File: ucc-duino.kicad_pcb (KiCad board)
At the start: 2 copper layers, 68.6 x 53.3 mm, 61 parts, among them J1 USB_OTG, J1-A1 Con1x8F, J1-B1 Con1x8F, J2 Con1x6F, J3 Con1x2F, J3-A1 Con1x8F, J3-B1 Con1x8F, J4 Con1x6F, J5 Con2x2CClocw, P5 CONN_01X01, P6 CONN_01X01, P7 CONN_01X01, P8 CONN_01X01, Q1 BC817, Q2 BC817, SW1 SW_Push, SW2 SW_Push, SW3 SW_USR, U1 STM32F103R4T6, U2 AP1117-33, Y1 OSC 8MHz, Y2 OSC 32768KHz

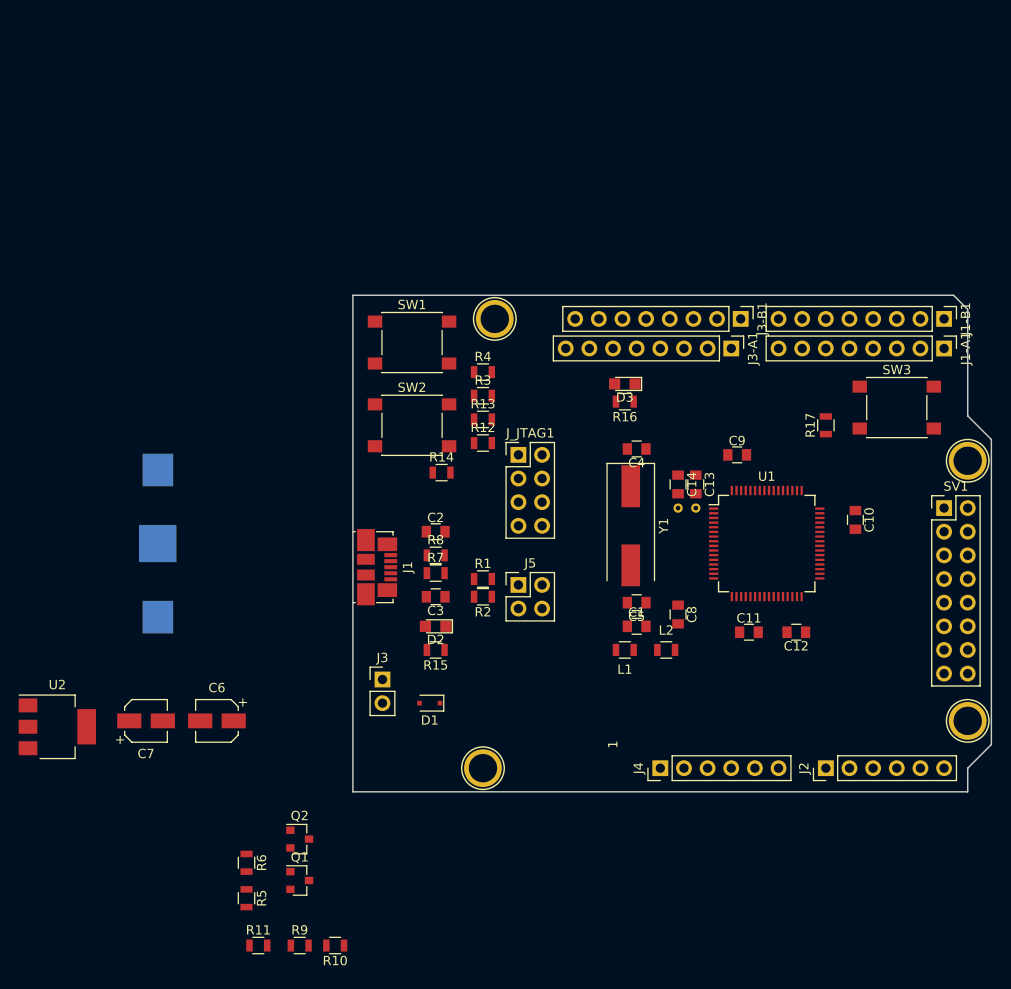
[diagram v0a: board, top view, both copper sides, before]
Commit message: Primeras pistas y leve reacomodación de componentes
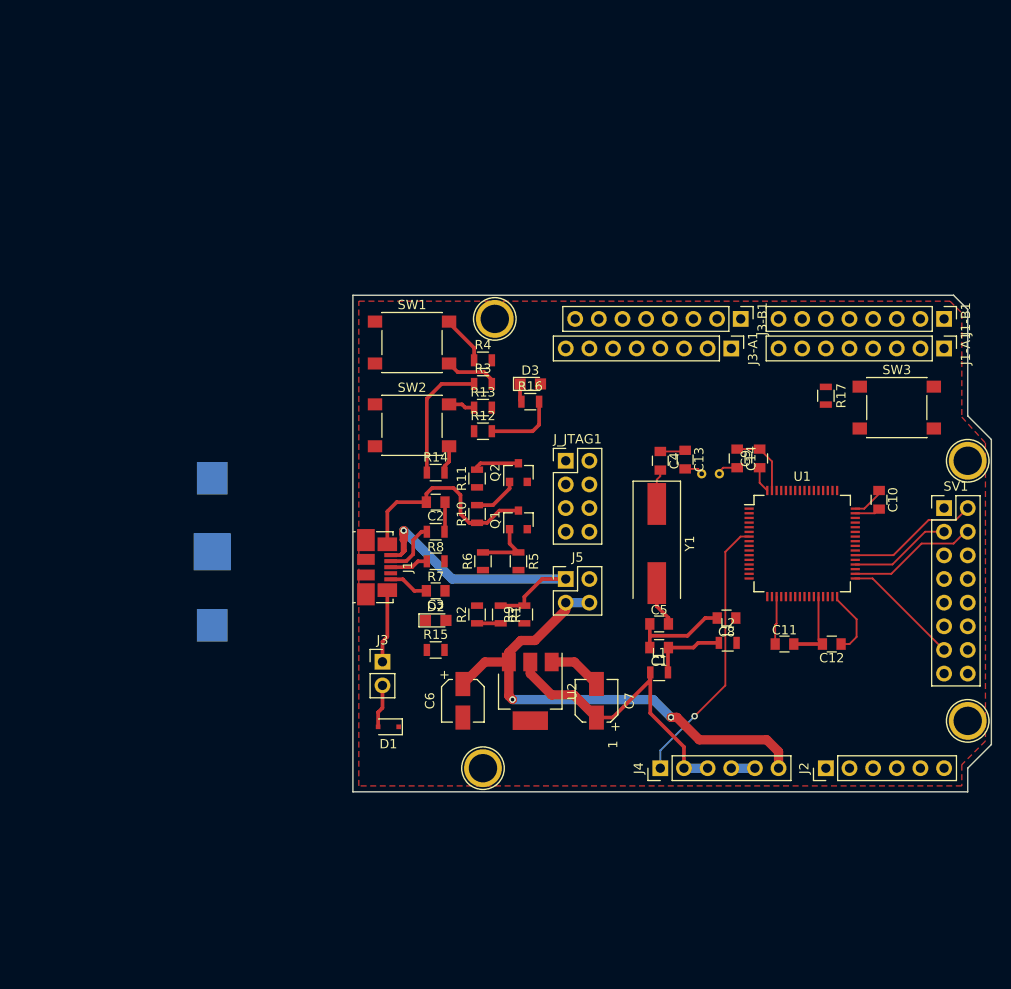
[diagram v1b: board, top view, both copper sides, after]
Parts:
- moved R11 55.4 mm to (123.7, 92.1), turned to 90 degrees
- moved U2 50.9 mm to (129.4, 114.9), turned to 270 degrees
- moved R10 48.8 mm to (123.7, 95.9), turned to 90 degrees
- moved C7 48.4 mm to (136.5, 116.0), turned to 90 degrees
- moved R5 46.5 mm to (128.1, 101.0)
- moved Q2 45.8 mm to (128.1, 91.4), turned to 90 degrees
- moved Q1 45.3 mm to (128.1, 96.5), turned to 90 degrees
- moved R9 43.0 mm to (128.8, 106.7), turned to 90 degrees
- moved R6 41.2 mm to (124.3, 101.0), turned to 90 degrees
- moved C6 26.5 mm to (122.2, 116.0), turned to 270 degrees
- moved D3 10.2 mm to (129.4, 81.9), turned to 0 degrees
- moved R16 10.2 mm to (129.4, 83.8), turned to 0 degrees
- moved C14 6.94 mm to (151.6, 89.9)
- moved L2 6.65 mm to (150.6, 109.7)
- moved BT1 5.91 mm to (95.2, 99.9), turned to 270 degrees
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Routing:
- net GND: track 0.00 -> 82.7 mm
- net VDD: track 0.00 -> 65.3 mm
- net /Vin: track 0.00 -> 55.1 mm, vias 0 -> 2
- net VBUS: track 0.00 -> 37.4 mm, vias 0 -> 1
- net /JTAG-TRST: track 0.00 -> 35.1 mm, vias 0 -> 1
- net /36: track 0.00 -> 14.2 mm
- net /32: track 0.00 -> 14.0 mm
- net /31: track 0.00 -> 12.7 mm
- net /34: track 0.00 -> 11.0 mm
- net Net-(C1-Pad1): track 0.00 -> 8.31 mm
- net Net-(Q1-Pad1): track 0.00 -> 6.70 mm
- net Net-(J1-Pad2): track 0.00 -> 6.08 mm
- net Net-(R4-Pad1): track 0.00 -> 5.27 mm
- net Net-(Q1-Pad2): track 0.00 -> 4.95 mm
- net Net-(Q2-Pad3): track 0.00 -> 4.92 mm
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- added copper zone on F.Cu, net GND
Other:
- net class 1mm added: clearance 0.3, trace_width 0.4, via_dia 0.8, via_drill 0.4
- net class Default: trace_width 0.25 -> 0.2; via_dia 0.6 -> 0.7
- net class Fino added: clearance 0.2, trace_width 0.2, via_dia 0.7, via_drill 0.4
- net class Mínimo MAYER added: clearance 0.125, trace_width 0.125, via_dia 0.7, via_drill 0.4
- net class normal added: clearance 0.4, trace_width 1, via_dia 1.2, via_drill 0.8
- rule trace_min: 0.2 -> 0.125
- rule via_min_drill: 0.3 -> 0.4
- rule via_min_size: 0.4 -> 0.7

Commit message: Pistas day 3
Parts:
- Y2: moved to F.Cu
- moved BT1 65.8 mm to (140.6, 52.3)
- moved C14 5.97 mm to (145.7, 90.2)
- moved C13 5.97 mm to (152.0, 89.9)
- moved D3 2.75 mm to (131.7, 83.4), turned to 270 degrees
- moved Y2 2.64 mm to (150.0, 93.1), turned to 180 degrees
- moved R2 1.02 mm to (122.7, 106.7)
- moved R16 0.64 mm to (128.9, 83.4), turned to 270 degrees
- turned R15 to 180 degrees
- turned R17 to 180 degrees
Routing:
- net GND: track 82.7 -> 278.3 mm, vias 0 -> 3
- net VDD: track 65.3 -> 164.6 mm
- net Net-(C3-Pad1): track 0.00 -> 77.8 mm, vias 0 -> 3
- net Net-(C2-Pad1): track 3.20 -> 60.0 mm, vias 0 -> 2
- net /BOOT0: track 2.83 -> 53.1 mm
- net Net-(R13-Pad2): track 0.00 -> 49.7 mm, vias 0 -> 2
- net /14: track 0.00 -> 37.5 mm, vias 0 -> 1
- net Net-(D1-Pad1): track 0.00 -> 33.1 mm, vias 0 -> 1
- net /8: track 0.00 -> 32.7 mm, vias 0 -> 1
- net /37: track 0.00 -> 30.2 mm, vias 0 -> 1
- net /JTAG-TRST: track 35.1 -> 63.9 mm
- net /7: track 0.00 -> 28.0 mm, vias 0 -> 1
- net /6: track 0.00 -> 27.8 mm, vias 0 -> 1
- net Net-(Q1-Pad2): track 4.95 -> 31.5 mm
- net /20: track 0.00 -> 24.6 mm, vias 0 -> 1
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
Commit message: Day4
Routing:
- net VDD: track 164.6 -> 185.0 mm, vias 0 -> 1
- net GND: track 278.3 -> 282.7 mm, vias 3 -> 4
- added copper zone on B.Cu, net GND

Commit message: 8 pistas to go
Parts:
- removed J_JTAG1: Con2x4CCw, Pin_Headers:Pin_Header_Straight_2x04_Pitch2.54mm
- added J-JTAG1: Con2x4Odd, Pin_Headers:Pin_Header_Straight_2x04_Pitch2.54mm, F.Cu at (133.2, 89.4)
- SV1: value Con2x8CCw -> Con2x8Odd
- moved SV1 18.0 mm to (176.4, 113.0), turned to 180 degrees
- moved C4 7.69 mm to (147.3, 96.8), turned to 90 degrees
- moved C5 7.54 mm to (147.3, 101.3), turned to 270 degrees
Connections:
- SV1 pad 1: GND -> /23
- SV1 pad 10: /25 -> /32
- SV1 pad 11: /27 -> /33
- SV1 pad 12: /29 -> /34
- SV1 pad 13: /31 -> /35
- SV1 pad 14: /33 -> /36
- SV1 pad 15: /35 -> /37
- SV1 pad 16: /37 -> GND
- SV1 pad 2: /36 -> /24
- SV1 pad 3: /34 -> /25
- SV1 pad 4: /32 -> /26
- SV1 pad 5: /30 -> /27
- SV1 pad 7: /26 -> /29
- SV1 pad 8: /24 -> /30
- SV1 pad 9: /23 -> /31
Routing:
- net GND: track 282.7 -> 371.4 mm, vias 4 -> 6
- net VDD: track 185.0 -> 251.6 mm, vias 1 -> 7
- net /25: track 0.00 -> 57.3 mm, vias 0 -> 1
- net /USB_P: track 3.56 -> 54.4 mm, vias 0 -> 4
- net /23: track 0.00 -> 50.4 mm, vias 0 -> 1
- net /24: track 0.00 -> 47.1 mm, vias 0 -> 1
- net /DISC: track 0.00 -> 45.0 mm, vias 0 -> 2
- net /JTAG-TDI: track 0.00 -> 40.0 mm, vias 0 -> 1
- net /JTAG-TMS: track 0.00 -> 39.4 mm, vias 0 -> 1
- net /JTAG-TCK: track 0.00 -> 38.5 mm, vias 0 -> 1
- net /0: track 0.00 -> 35.9 mm, vias 0 -> 1
- net /3: track 0.00 -> 35.6 mm, vias 0 -> 1
- net /1: track 0.00 -> 34.9 mm, vias 0 -> 1
- net /2: track 0.00 -> 33.3 mm, vias 0 -> 2
- net /JTAG-TDO: track 0.00 -> 33.1 mm, vias 0 -> 1
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
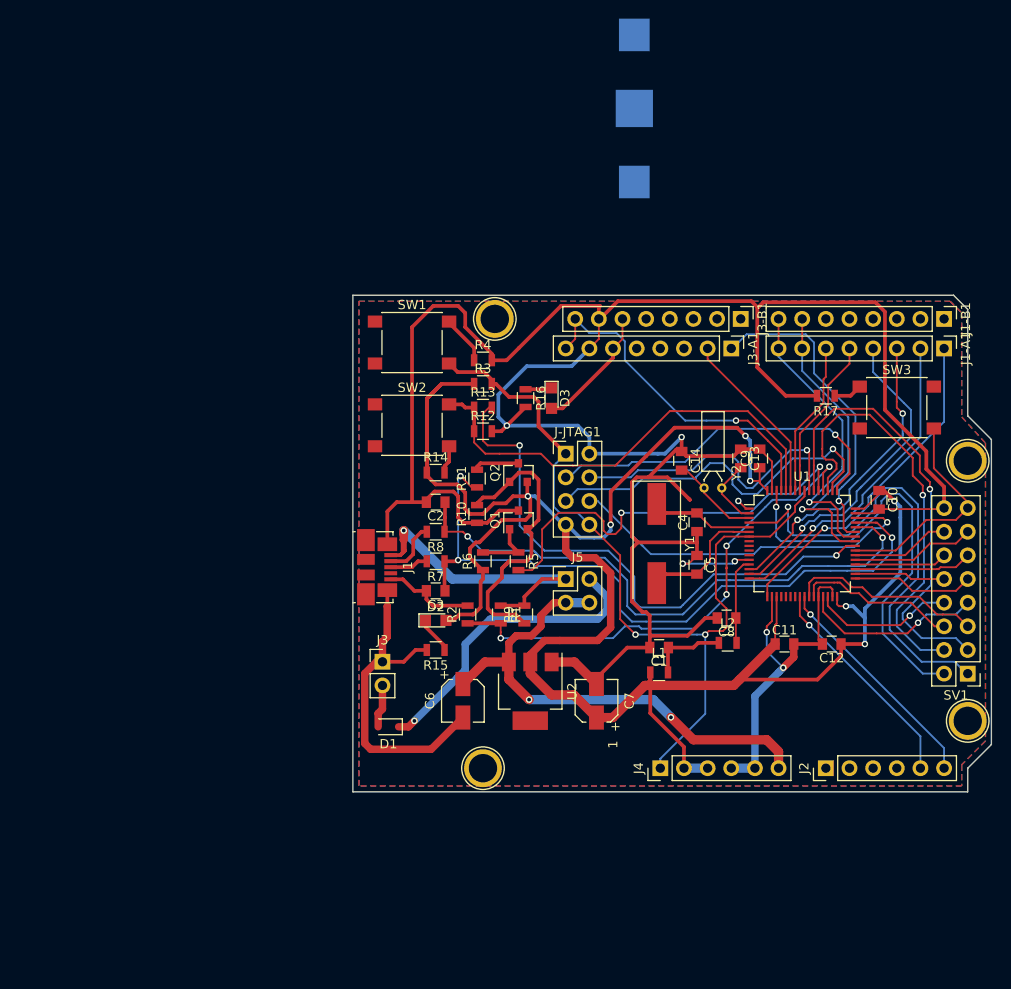
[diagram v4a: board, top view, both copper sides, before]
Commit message: Fin de ruteo
faltan fiduciarios y texto
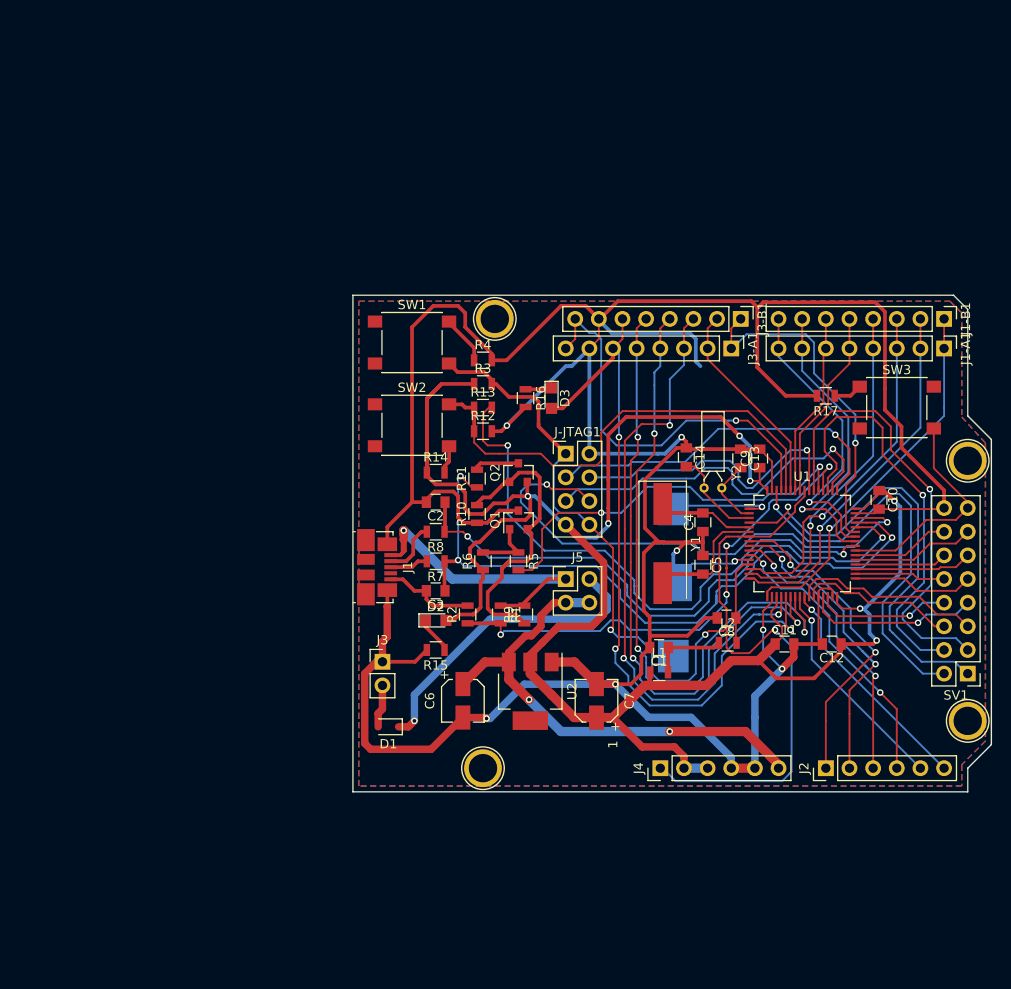
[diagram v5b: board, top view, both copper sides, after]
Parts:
- moved BT1 51.1 mm to (144.8, 103.3)
- moved C4 0.64 mm to (148.0, 96.8)
- moved C5 0.64 mm to (148.0, 101.3)
- moved Y1 0.63 mm to (143.6, 99.1)
- moved C14 0.63 mm to (146.2, 89.8)
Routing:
- net /11: track 0.00 -> 69.8 mm, vias 0 -> 3
- net /10: track 0.00 -> 68.9 mm, vias 0 -> 3
- net /12: track 0.00 -> 67.1 mm, vias 0 -> 3
- net /13: track 13.5 -> 79.5 mm, vias 0 -> 3
- net GND: track 371.4 -> 414.8 mm, vias 6 -> 8
- net /15: track 0.00 -> 34.9 mm, vias 0 -> 2
- net /16: track 0.00 -> 34.6 mm, vias 0 -> 2
- net /JTAG-TRST: track 91.5 -> 123.4 mm, vias 2 -> 3
- net /17: track 0.00 -> 31.6 mm, vias 0 -> 2
- net /18: track 0.00 -> 31.2 mm, vias 0 -> 2
- net VDD: track 251.6 -> 233.0 mm
- net /JTAG-TMS: track 39.4 -> 57.5 mm, vias 1 -> 2
- net /VBAT: track 1.50 -> 11.5 mm
- net /14: track 36.8 -> 43.6 mm
- net /1: track 34.9 -> 39.2 mm
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
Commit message: Lista para revisión1
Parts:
- added R1: Fiducial_1mm_Dia_2.54mm_Outer_CopperTop, Fiducials:Fiducial_1mm_Dia_2.54mm_Outer_CopperTop, F.Cu at (113.2, 123.2)
- added R2: Fiducial_1mm_Dia_2.54mm_Outer_CopperTop, Fiducials:Fiducial_1mm_Dia_2.54mm_Outer_CopperTop, F.Cu at (116.0, 77.2)
- added R3: Fiducial_1mm_Dia_2.54mm_Outer_CopperTop, Fiducials:Fiducial_1mm_Dia_2.54mm_Outer_CopperTop, F.Cu at (174.2, 85.2)
- moved SW1 0.76 mm to (168.8, 85.2)
- moved R11 0.64 mm to (123.7, 91.4)
- moved ? 0.51 mm to (173.9, 78.6)
- moved ? 0.51 mm to (151.0, 78.6)
- moved C13 0.13 mm to (151.9, 89.9)
- renumbered J1 to ?, J1-A1 to ?, J1-B1 to ?, J2 to ?, J3-A1 to ?, J3-B1 to ?, J4 to ?, J5 to ?, SV1 to ?, SW2 to BOOT, SW1 to RST, SW3 to SW1
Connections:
- ? pad 3: VDD -> VDDA
- C8 pad 1: /VDDA -> VDDA
- L2 pad 2: /VDDA -> VDDA
- U1 pad 13: /VDDA -> VDDA
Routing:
- net VDDA: track 0.00 -> 31.0 mm, vias 0 -> 2
- net GND: track 414.8 -> 425.4 mm
- net /VDDA: track 9.40 -> 0.00 mm
- net VDD: track 233.0 -> 228.2 mm
- net /USB_P: track 55.3 -> 57.2 mm
- net /8: track 36.9 -> 35.9 mm
- net Net-(Q2-Pad3): track 4.92 -> 4.08 mm
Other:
- board text added: "0"
- board text added: "10"
- board text added: "11"
- board text added: "12"
- board text added: "13"
- board text added: "14"
- board text added: "2"
- board text added: "23"
- board text added: "24"
- board text added: "25"
- board text added: "26"
- board text added: "27"
- board text added: "28"
- board text added: "29"
- board text added: "3"
- board text added: "30"
- board text added: "31"
- board text added: "32"
- board text added: "33"
- board text added: "34"
- board text added: "35"
- board text added: "36"
- board text added: "37"
- board text added: "4"
- board text added: "5"
- board text added: "6"
- board text added: "7"
- board text added: "8"
- board text added: "9"
- board text added: "Ain15"
- board text added: "Ain16"
- board text added: "Ain17"
- board text added: "Ain18"
- board text added: "Ain19"
- board text added: "Ain20"
- board text added: "EXT"
- board text added: "GND"
- board text added: "J-RST"
- board text added: "TCK"
- board text added: "TDI"
- board text added: "TDO"
- board text added: "TMS"
- board text added: "TRST"
- board text added: "USB"
- board text added: "VDD"
- board text added: "VDDA"
- board text added: "Vext"
- board text added: "Vin"

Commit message: Algunos retoques
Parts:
- added R3: Fiducial_1mm_Dia_2.54mm_Outer_CopperTop, Fiducials:Fiducial_1mm_Dia_2.54mm_Outer_CopperTop, F.Cu at (152.4, 93.5)
- moved D3 5.04 mm to (128.9, 79.2), turned to 0 degrees
- renumbered D2 to PWR
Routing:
- net GND: track 425.4 -> 437.1 mm, vias 8 -> 9
- net VDDA: track 31.0 -> 27.2 mm
- net /JTAG-TDI: track 39.6 -> 38.5 mm
- net Net-(D3-Pad1): track 2.86 -> 3.91 mm
- net /Vin: track 53.5 -> 54.5 mm
- net VDD: track 228.2 -> 227.3 mm
- net /JTAG-TDO: track 32.4 -> 31.8 mm

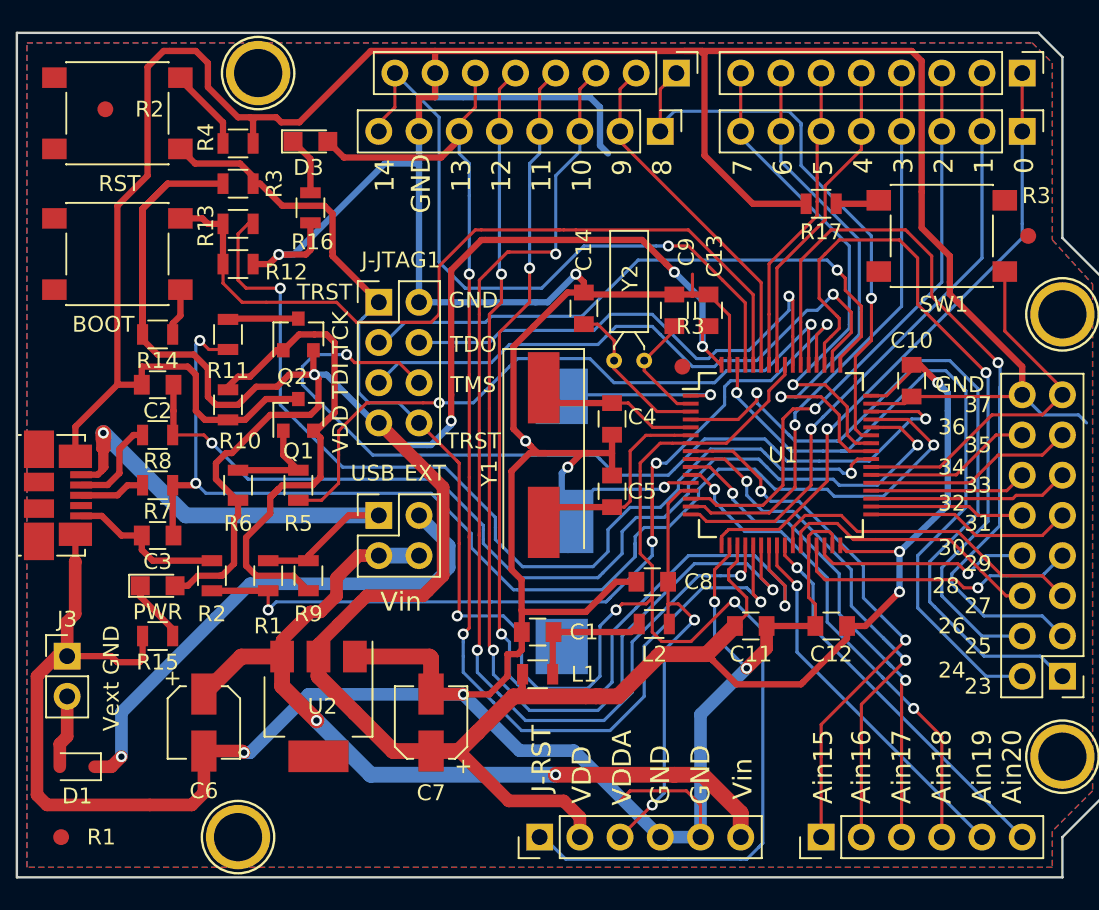
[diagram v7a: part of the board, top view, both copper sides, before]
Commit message: BOM y valores de componentes
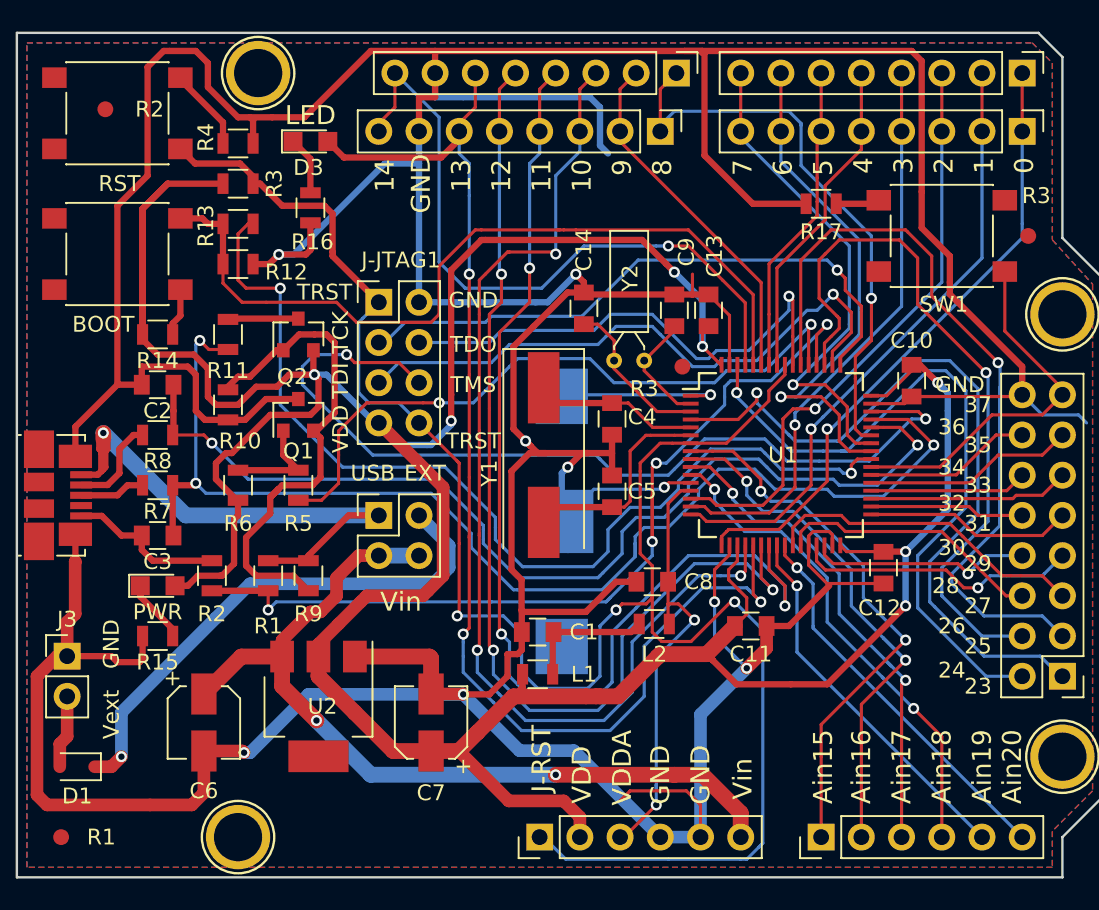
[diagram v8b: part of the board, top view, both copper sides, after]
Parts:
- moved C12 4.95 mm to (165.1, 106.2), turned to 270 degrees
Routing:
- net GND: track 437.1 -> 439.9 mm
- net VDD: track 227.3 -> 228.0 mm
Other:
- board text added: "LED"
